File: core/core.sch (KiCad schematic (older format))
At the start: 153 parts, among them K0 KEYSW, K1 KEYSW, K10 KEYSW, K11 KEYSW, K12 KEYSW, K13 KEYSW, K14 KEYSW, K15 KEYSW, K16 KEYSW, K17 KEYSW, K18 KEYSW, K19 KEYSW, K2 KEYSW, K20 KEYSW, K21 KEYSW, K22 KEYSW, K23 KEYSW, K24 KEYSW, K25 KEYSW, K26 KEYSW, K27 KEYSW, K28 KEYSW, K29 KEYSW, K3 KEYSW, K30 KEYSW, K31 KEYSW, K32 KEYSW, K33 KEYSW, K34 KEYSW, K35 KEYSW, K36 KEYSW, K37 KEYSW, K38 KEYSW, K39 KEYSW, K4 KEYSW, K40 KEYSW, K41 KEYSW, K42 KEYSW, K43 KEYSW, K44 KEYSW, K45 KEYSW, K46 KEYSW, K47 KEYSW, K48 KEYSW, K49 KEYSW, K5 KEYSW, K50 KEYSW, K51 KEYSW, K52 KEYSW, K53 KEYSW, K54 KEYSW, K55 KEYSW, K56 KEYSW, K57 KEYSW, K58 KEYSW, K59 KEYSW, K6 KEYSW, K60 KEYSW, K61 KEYSW, K62 KEYSW, K63 KEYSW, K64 KEYSW, K65 KEYSW, K66 KEYSW, K67 KEYSW, K68 KEYSW, K69 KEYSW, K7 KEYSW, K8 KEYSW, K9 KEYSW, U1. Teensy-LC

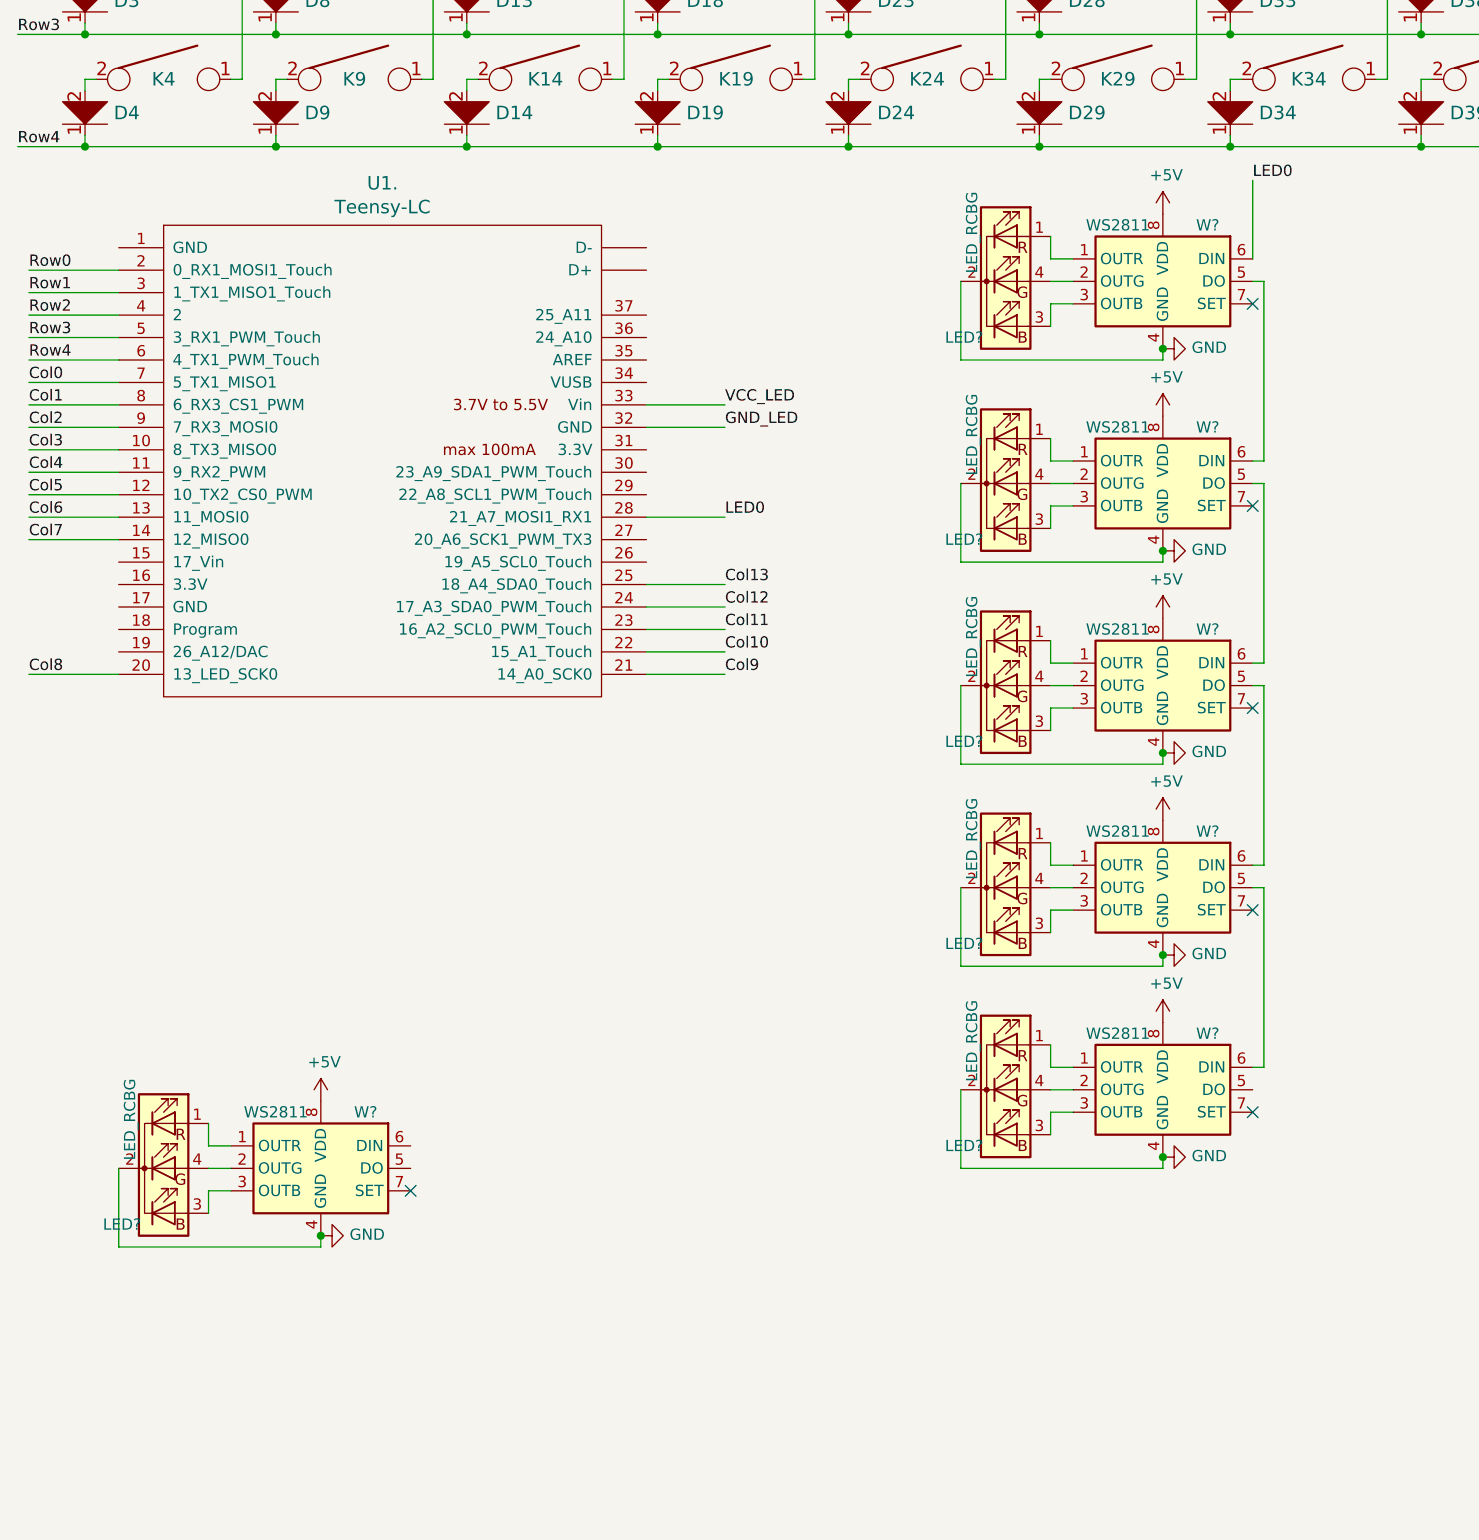
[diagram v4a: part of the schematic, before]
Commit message: Changed pin assignments, cleaned up RGB LEDs
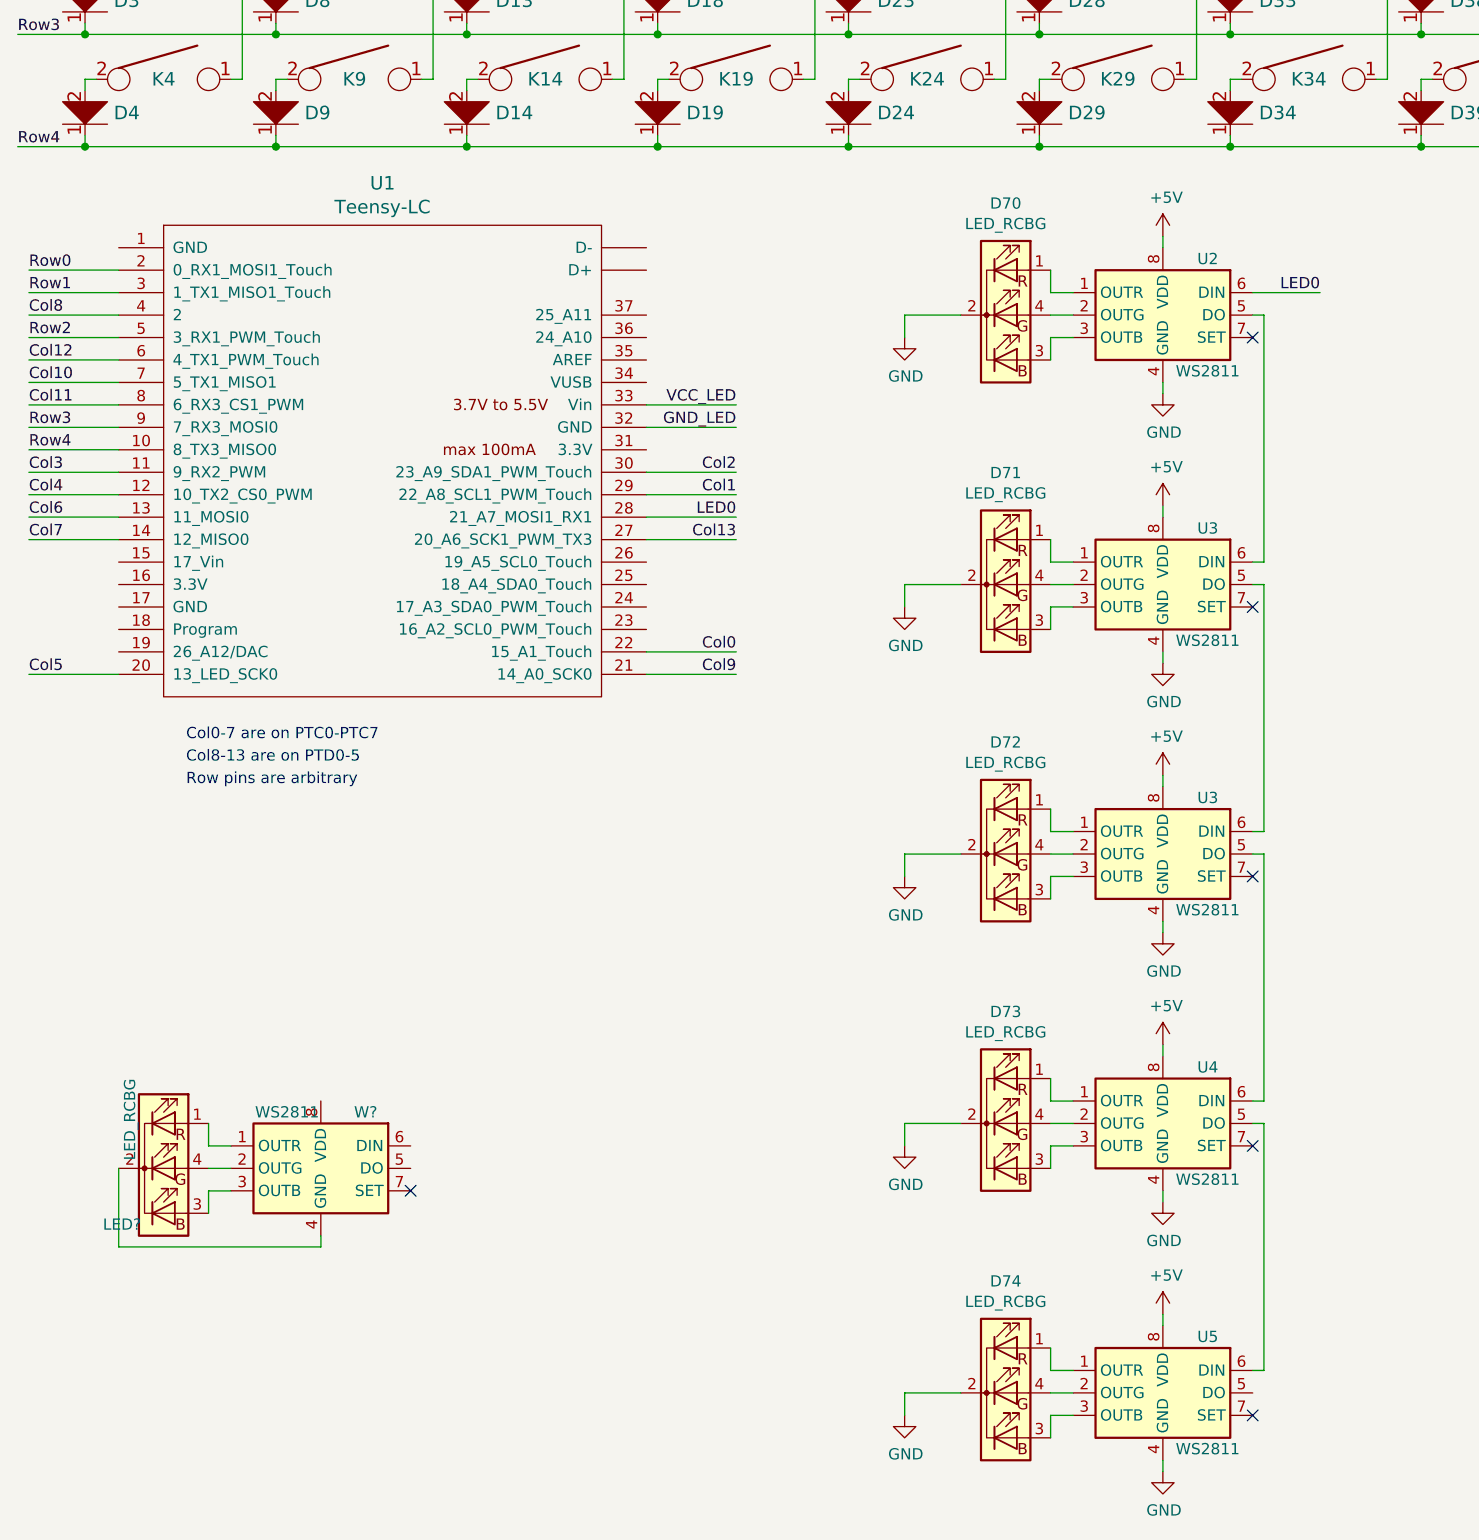
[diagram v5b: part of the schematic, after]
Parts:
- removed LED? (x5): LED_RCBG, Connector_PinHeader_1.00mm:PinHeader_1x04_P1.00mm_Horizontal, symbol Device:LED_RCBG
- removed W? (x5): WS2811, Package_SO:SOIC-8-1EP_3.9x4.9mm_P1.27mm_EP2.29x3mm, symbol Driver_LED:WS2811
- added D70, D71, D72, D73, D74: LED_RCBG, Connector_PinHeader_1.00mm:PinHeader_1x04_P1.00mm_Horizontal, symbol Device:LED_RCBG
- added U2, U3 (x2), U4, U5: WS2811, Package_SO:SOIC-8-1EP_3.9x4.9mm_P1.27mm_EP2.29x3mm, symbol Driver_LED:WS2811
- renumbered U1. to U1
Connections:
- net +5V: now also U2.8 (VDD), U3.8 (VDD), U3.8 (VDD), U4.8 (VDD), U5.8 (VDD); no longer W?.8 (VDD)
- net Col0: now also U1.22 (15_A1_Touch); no longer U1.7 (5_TX1_MISO1)
- net Col1: now also U1.29 (22_A8_SCL1_PWM_Touch); no longer U1.8 (6_RX3_CS1_PWM)
- net Col10: now also U1.7 (5_TX1_MISO1); no longer U1.22 (15_A1_Touch)
- net Col11: now also U1.8 (6_RX3_CS1_PWM); no longer U1.23 (16_A2_SCL0_PWM_Touch)
- net Col12: now also U1.6 (4_TX1_PWM_Touch); no longer U1.24 (17_A3_SDA0_PWM_Touch)
- net Col13: now also U1.27 (20_A6_SCK1_PWM_TX3); no longer U1.25 (18_A4_SDA0_Touch)
- net Col2: now also U1.30 (23_A9_SDA1_PWM_Touch); no longer U1.9 (7_RX3_MOSI0)
- net Col3: now also U1.11 (9_RX2_PWM); no longer U1.10 (8_TX3_MISO0)
- net Col4: now also U1.12 (10_TX2_CS0_PWM); no longer U1.11 (9_RX2_PWM)
- net Col5: now also U1.20 (13_LED_SCK0); no longer U1.12 (10_TX2_CS0_PWM)
- net Col8: now also U1.4 (2); no longer U1.20 (13_LED_SCK0)
- net GND: now also D70.2 (K), D71.2 (K), D72.2 (K), D73.2 (K), D74.2 (K), U2.4 (GND), U3.4 (GND), U3.4 (GND), U4.4 (GND), U5.4 (GND); no longer LED?.2 (K), W?.4 (GND)
- net LED0: now also U2.6 (DIN)
- net Row2: now also U1.5 (3_RX1_PWM_Touch); no longer U1.4 (2)
- net Row3: now also U1.9 (7_RX3_MOSI0); no longer U1.5 (3_RX1_PWM_Touch)
- net Row4: now also U1.10 (8_TX3_MISO0); no longer U1.6 (4_TX1_PWM_Touch)
- new net: D70.1 (RA), U2.1 (OUTR)
- new net: D70.4 (GA), U2.2 (OUTG)
- new net: D70.3 (BA), U2.3 (OUTB)
- new net: U2.5 (DO), U3.6 (DIN)
- new net: D71.1 (RA), U3.1 (OUTR)
- new net: D71.4 (GA), U3.2 (OUTG)
- new net: D71.3 (BA), U3.3 (OUTB)
- new net: U3.5 (DO), U3.6 (DIN)
- new net: D72.1 (RA), U3.1 (OUTR)
- new net: D72.4 (GA), U3.2 (OUTG)
- new net: D72.3 (BA), U3.3 (OUTB)
- new net: U3.5 (DO), U4.6 (DIN)
- new net: D73.1 (RA), U4.1 (OUTR)
- new net: D73.4 (GA), U4.2 (OUTG)
- new net: D73.3 (BA), U4.3 (OUTB)
- new net: U4.5 (DO), U5.6 (DIN)
- new net: D74.1 (RA), U5.1 (OUTR)
- new net: D74.4 (GA), U5.2 (OUTG)
- new net: D74.3 (BA), U5.3 (OUTB)
- new net: LED?.2 (K), W?.4 (GND)
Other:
- note added: "Col0-7 are on PTC0-PTC7"
- note added: "Col8-13 are on PTD0-5"
- note added: "Row pins are arbitrary"

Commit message: LED chain of horrors
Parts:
- removed LED?: LED_RCBG, Connector_PinHeader_1.00mm:PinHeader_1x04_P1.00mm_Horizontal, symbol Device:LED_RCBG
- removed U3 (x2), W?: WS2811, Package_SO:SOIC-8-1EP_3.9x4.9mm_P1.27mm_EP2.29x3mm, symbol Driver_LED:WS2811
- added D100, D101, D102, D103, D104, D105, D106, D107, D108, D109, D110, D111, D112, D113, D114, D115, D116, D117, D118, D119, D120, D121, D122, D123, D124, D125, D126, D127, D128, D129, D130, D131, D132, D133, D134, D135, D136, D137, D138, D139, D140, D75, D76, D77, D78, D79, D80, D81, D82, D83, D84, D85, D86, D87, D88, D89, D90, D91, D92, D93, D94, D95, D96, D97, D98, D99: LED_RCBG, Connector_PinHeader_1.00mm:PinHeader_1x04_P1.00mm_Horizontal, symbol Device:LED_RCBG
- added U10, U11, U12, U13, U14, U15, U16, U17, U18, U19, U20, U21, U22, U23, U24, U25, U26, U27, U28, U29, U3, U30, U31, U32, U33, U34, U35, U36, U37, U38, U39, U40, U41, U42, U43, U44, U45, U46, U47, U48, U49, U50, U51, U52, U53, U54, U55, U56, U57, U58, U59, U6, U60, U61, U62, U63, U64, U65, U66, U67, U68, U69, U7, U70, U71, U72, U8, U9: WS2811, Package_SO:SOIC-8-1EP_3.9x4.9mm_P1.27mm_EP2.29x3mm, symbol Driver_LED:WS2811
- U1: footprint (none) -> teensy:Teensy30_31_32_LC
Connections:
- net Row1 is gone; now on net Col3: D1.1, D11.1, D16.1, D21.1, D26.1, D31.1, D36.1, D41.1, D46.1, D51.1, D56.1, D6.1, D61.1, D66.1, U1.3 (1_TX1_MISO1_Touch)
- net Row2 is gone; now on net Col3: D12.1, D17.1, D2.1, D22.1, D27.1, D32.1, D37.1, D42.1, D47.1, D52.1, D57.1, D62.1, D67.1, D7.1, U1.5 (3_RX1_PWM_Touch)
- net +5V: now also U10.8 (VDD), U11.8 (VDD), U12.8 (VDD), U13.8 (VDD), U14.8 (VDD), U15.8 (VDD), U16.8 (VDD), U17.8 (VDD), U18.8 (VDD), U19.8 (VDD), U20.8 (VDD), U21.8 (VDD), U22.8 (VDD), U23.8 (VDD), U24.8 (VDD), U25.8 (VDD), U26.8 (VDD), U27.8 (VDD), U28.8 (VDD), U29.8 (VDD), U3.8 (VDD), U30.8 (VDD), U31.8 (VDD), U32.8 (VDD), U33.8 (VDD), U34.8 (VDD), U35.8 (VDD), U36.8 (VDD), U37.8 (VDD), U38.8 (VDD), U39.8 (VDD), U40.8 (VDD), U41.8 (VDD), U42.8 (VDD), U43.8 (VDD), U44.8 (VDD), U45.8 (VDD), U46.8 (VDD), U47.8 (VDD), U48.8 (VDD), U49.8 (VDD), U50.8 (VDD), U51.8 (VDD), U52.8 (VDD), U53.8 (VDD), U54.8 (VDD), U55.8 (VDD), U56.8 (VDD), U57.8 (VDD), U58.8 (VDD), U59.8 (VDD), U6.8 (VDD), U60.8 (VDD), U61.8 (VDD), U62.8 (VDD), U63.8 (VDD), U64.8 (VDD), U65.8 (VDD), U66.8 (VDD), U67.8 (VDD), U68.8 (VDD), U69.8 (VDD), U7.8 (VDD), U70.8 (VDD), U71.8 (VDD), U72.8 (VDD), U8.8 (VDD), U9.8 (VDD)
- net GND: now also D100.2 (K), D101.2 (K), D102.2 (K), D103.2 (K), D104.2 (K), D105.2 (K), D106.2 (K), D107.2 (K), D108.2 (K), D109.2 (K), D110.2 (K), D111.2 (K), D112.2 (K), D113.2 (K), D114.2 (K), D115.2 (K), D116.2 (K), D117.2 (K), D118.2 (K), D119.2 (K), D120.2 (K), D121.2 (K), D122.2 (K), D123.2 (K), D124.2 (K), D125.2 (K), D126.2 (K), D127.2 (K), D128.2 (K), D129.2 (K), D130.2 (K), D131.2 (K), D132.2 (K), D133.2 (K), D134.2 (K), D135.2 (K), D136.2 (K), D137.2 (K), D138.2 (K), D139.2 (K), D140.2 (K), D75.2 (K), D76.2 (K), D77.2 (K), D78.2 (K), D79.2 (K), D80.2 (K), D81.2 (K), D82.2 (K), D83.2 (K), D84.2 (K), D85.2 (K), D86.2 (K), D87.2 (K), D88.2 (K), D89.2 (K), D90.2 (K), D91.2 (K), D92.2 (K), D93.2 (K), D94.2 (K), D95.2 (K), D96.2 (K), D97.2 (K), D98.2 (K), D99.2 (K), U10.4 (GND), U11.4 (GND), U12.4 (GND), U13.4 (GND), U14.4 (GND), U15.4 (GND), U16.4 (GND), U17.4 (GND), U18.4 (GND), U19.4 (GND), U20.4 (GND), U21.4 (GND), U22.4 (GND), U23.4 (GND), U24.4 (GND), U25.4 (GND), U26.4 (GND), U27.4 (GND), U28.4 (GND), U29.4 (GND), U3.4 (GND), U30.4 (GND), U31.4 (GND), U32.4 (GND), U33.4 (GND), U34.4 (GND), U35.4 (GND), U36.4 (GND), U37.4 (GND), U38.4 (GND), U39.4 (GND), U40.4 (GND), U41.4 (GND), U42.4 (GND), U43.4 (GND), U44.4 (GND), U45.4 (GND), U46.4 (GND), U47.4 (GND), U48.4 (GND), U49.4 (GND), U50.4 (GND), U51.4 (GND), U52.4 (GND), U53.4 (GND), U54.4 (GND), U55.4 (GND), U56.4 (GND), U57.4 (GND), U58.4 (GND), U59.4 (GND), U6.4 (GND), U60.4 (GND), U61.4 (GND), U62.4 (GND), U63.4 (GND), U64.4 (GND), U65.4 (GND), U66.4 (GND), U67.4 (GND), U68.4 (GND), U69.4 (GND), U7.4 (GND), U70.4 (GND), U71.4 (GND), U72.4 (GND), U8.4 (GND), U9.4 (GND)
- net at U2.5 (DO): now also U3.6 (DIN)
- net at D71.1 (RA): now also U3.1 (OUTR)
- net at D71.4 (GA): now also U3.2 (OUTG)
- net at D71.3 (BA): now also U3.3 (OUTB)
- net at D72.1 (RA): now also U4.1 (OUTR)
- net at D72.4 (GA): now also U4.2 (OUTG)
- net at D72.3 (BA): now also U4.3 (OUTB)
- net at U4.6 (DIN): now also U3.5 (DO)
- net at D73.1 (RA): now also U5.1 (OUTR); no longer U4.1 (OUTR)
- net at D73.4 (GA): now also U5.2 (OUTG); no longer U4.2 (OUTG)
- net at D73.3 (BA): now also U5.3 (OUTB); no longer U4.3 (OUTB)
- net at D74.1 (RA): now also U6.1 (OUTR); no longer U5.1 (OUTR)
- net at D74.4 (GA): now also U6.2 (OUTG); no longer U5.2 (OUTG)
- net at D74.3 (BA): now also U6.3 (OUTB); no longer U5.3 (OUTB)
- net at U5.5 (DO): now also U6.6 (DIN)
- new net: D140.1 (RA), U72.1 (OUTR)
- new net: D140.4 (GA), U72.2 (OUTG)
- new net: D140.3 (BA), U72.3 (OUTB)
- new net: U6.5 (DO), U7.6 (DIN)
- new net: D79.1 (RA), U11.1 (OUTR)
- new net: D79.3 (BA), U11.3 (OUTB)
- new net: D79.4 (GA), U11.2 (OUTG)
- new net: U11.5 (DO), U12.6 (DIN)
- new net: U10.5 (DO), U11.6 (DIN)
- new net: D78.1 (RA), U10.1 (OUTR)
- new net: D78.3 (BA), U10.3 (OUTB)
- new net: D78.4 (GA), U10.2 (OUTG)
- new net: U10.6 (DIN), U9.5 (DO)
- new net: D77.1 (RA), U9.1 (OUTR)
- new net: D77.3 (BA), U9.3 (OUTB)
- new net: D77.4 (GA), U9.2 (OUTG)
- new net: U8.5 (DO), U9.6 (DIN)
- new net: D76.1 (RA), U8.1 (OUTR)
- new net: D76.3 (BA), U8.3 (OUTB)
- new net: D76.4 (GA), U8.2 (OUTG)
- new net: U7.5 (DO), U8.6 (DIN)
- new net: D75.1 (RA), U7.1 (OUTR)
- new net: D75.3 (BA), U7.3 (OUTB)
- new net: D75.4 (GA), U7.2 (OUTG)
- new net: D84.1 (RA), U16.1 (OUTR)
- new net: D84.3 (BA), U16.3 (OUTB)
- new net: D84.4 (GA), U16.2 (OUTG)
- new net: U16.5 (DO), U17.6 (DIN)
- new net: U15.5 (DO), U16.6 (DIN)
- new net: D83.1 (RA), U15.1 (OUTR)
- new net: D83.3 (BA), U15.3 (OUTB)
- new net: D83.4 (GA), U15.2 (OUTG)
- new net: U14.5 (DO), U15.6 (DIN)
- new net: D82.1 (RA), U14.1 (OUTR)
- new net: D82.3 (BA), U14.3 (OUTB)
- new net: D82.4 (GA), U14.2 (OUTG)
- new net: U13.5 (DO), U14.6 (DIN)
- new net: D81.1 (RA), U13.1 (OUTR)
- new net: D81.3 (BA), U13.3 (OUTB)
- new net: D81.4 (GA), U13.2 (OUTG)
- new net: U12.5 (DO), U13.6 (DIN)
- new net: D80.1 (RA), U12.1 (OUTR)
- new net: D80.3 (BA), U12.3 (OUTB)
- new net: D80.4 (GA), U12.2 (OUTG)
- new net: D89.1 (RA), U21.1 (OUTR)
- new net: D89.3 (BA), U21.3 (OUTB)
- new net: D89.4 (GA), U21.2 (OUTG)
- new net: U21.5 (DO), U22.6 (DIN)
- new net: U20.5 (DO), U21.6 (DIN)
- new net: D88.1 (RA), U20.1 (OUTR)
- new net: D88.3 (BA), U20.3 (OUTB)
- new net: D88.4 (GA), U20.2 (OUTG)
- new net: U19.5 (DO), U20.6 (DIN)
- new net: D87.1 (RA), U19.1 (OUTR)
- new net: D87.3 (BA), U19.3 (OUTB)
- new net: D87.4 (GA), U19.2 (OUTG)
- new net: U18.5 (DO), U19.6 (DIN)
- new net: D86.1 (RA), U18.1 (OUTR)
- new net: D86.3 (BA), U18.3 (OUTB)
- new net: D86.4 (GA), U18.2 (OUTG)
- new net: U17.5 (DO), U18.6 (DIN)
- new net: D85.1 (RA), U17.1 (OUTR)
- new net: D85.3 (BA), U17.3 (OUTB)
- new net: D85.4 (GA), U17.2 (OUTG)
- new net: D94.1 (RA), U26.1 (OUTR)
- new net: D94.3 (BA), U26.3 (OUTB)
- new net: D94.4 (GA), U26.2 (OUTG)
- new net: U26.5 (DO), U27.6 (DIN)
- new net: U25.5 (DO), U26.6 (DIN)
- new net: D93.1 (RA), U25.1 (OUTR)
- new net: D93.3 (BA), U25.3 (OUTB)
- new net: D93.4 (GA), U25.2 (OUTG)
- new net: U24.5 (DO), U25.6 (DIN)
- new net: D92.1 (RA), U24.1 (OUTR)
- new net: D92.3 (BA), U24.3 (OUTB)
- new net: D92.4 (GA), U24.2 (OUTG)
- new net: U23.5 (DO), U24.6 (DIN)
- new net: D91.1 (RA), U23.1 (OUTR)
- new net: D91.3 (BA), U23.3 (OUTB)
- new net: D91.4 (GA), U23.2 (OUTG)
- new net: U22.5 (DO), U23.6 (DIN)
- new net: D90.1 (RA), U22.1 (OUTR)
- new net: D90.3 (BA), U22.3 (OUTB)
- new net: D90.4 (GA), U22.2 (OUTG)
- new net: D99.1 (RA), U31.1 (OUTR)
- new net: D99.3 (BA), U31.3 (OUTB)
- new net: D99.4 (GA), U31.2 (OUTG)
- new net: U31.5 (DO), U32.6 (DIN)
- new net: U30.5 (DO), U31.6 (DIN)
- new net: D98.1 (RA), U30.1 (OUTR)
- new net: D98.3 (BA), U30.3 (OUTB)
- new net: D98.4 (GA), U30.2 (OUTG)
- new net: U29.5 (DO), U30.6 (DIN)
- new net: D97.1 (RA), U29.1 (OUTR)
- new net: D97.3 (BA), U29.3 (OUTB)
- new net: D97.4 (GA), U29.2 (OUTG)
- new net: U28.5 (DO), U29.6 (DIN)
- new net: D96.1 (RA), U28.1 (OUTR)
- new net: D96.3 (BA), U28.3 (OUTB)
- new net: D96.4 (GA), U28.2 (OUTG)
- new net: U27.5 (DO), U28.6 (DIN)
- new net: D95.1 (RA), U27.1 (OUTR)
- new net: D95.3 (BA), U27.3 (OUTB)
- new net: D95.4 (GA), U27.2 (OUTG)
- new net: D104.1 (RA), U36.1 (OUTR)
- new net: D104.3 (BA), U36.3 (OUTB)
- new net: D104.4 (GA), U36.2 (OUTG)
- new net: U36.5 (DO), U37.6 (DIN)
- new net: U35.5 (DO), U36.6 (DIN)
- new net: D103.1 (RA), U35.1 (OUTR)
- new net: D103.3 (BA), U35.3 (OUTB)
- new net: D103.4 (GA), U35.2 (OUTG)
- new net: U34.5 (DO), U35.6 (DIN)
- new net: D102.1 (RA), U34.1 (OUTR)
- new net: D102.3 (BA), U34.3 (OUTB)
- new net: D102.4 (GA), U34.2 (OUTG)
- new net: U33.5 (DO), U34.6 (DIN)
- new net: D101.1 (RA), U33.1 (OUTR)
- new net: D101.3 (BA), U33.3 (OUTB)
- new net: D101.4 (GA), U33.2 (OUTG)
- new net: U32.5 (DO), U33.6 (DIN)
- new net: D100.1 (RA), U32.1 (OUTR)
- new net: D100.3 (BA), U32.3 (OUTB)
- new net: D100.4 (GA), U32.2 (OUTG)
- new net: D109.1 (RA), U41.1 (OUTR)
- new net: D109.3 (BA), U41.3 (OUTB)
- new net: D109.4 (GA), U41.2 (OUTG)
- new net: U41.5 (DO), U42.6 (DIN)
- new net: U40.5 (DO), U41.6 (DIN)
- new net: D108.1 (RA), U40.1 (OUTR)
- new net: D108.3 (BA), U40.3 (OUTB)
- new net: D108.4 (GA), U40.2 (OUTG)
- new net: U39.5 (DO), U40.6 (DIN)
- new net: D107.1 (RA), U39.1 (OUTR)
- new net: D107.3 (BA), U39.3 (OUTB)
- new net: D107.4 (GA), U39.2 (OUTG)
- new net: U38.5 (DO), U39.6 (DIN)
- new net: D106.1 (RA), U38.1 (OUTR)
- new net: D106.3 (BA), U38.3 (OUTB)
- new net: D106.4 (GA), U38.2 (OUTG)
- new net: U37.5 (DO), U38.6 (DIN)
- new net: D105.1 (RA), U37.1 (OUTR)
- new net: D105.3 (BA), U37.3 (OUTB)
- new net: D105.4 (GA), U37.2 (OUTG)
- new net: D114.1 (RA), U46.1 (OUTR)
- new net: D114.3 (BA), U46.3 (OUTB)
- new net: D114.4 (GA), U46.2 (OUTG)
- new net: U46.5 (DO), U47.6 (DIN)
- new net: U45.5 (DO), U46.6 (DIN)
- new net: D113.1 (RA), U45.1 (OUTR)
- new net: D113.3 (BA), U45.3 (OUTB)
- new net: D113.4 (GA), U45.2 (OUTG)
- new net: U44.5 (DO), U45.6 (DIN)
- new net: D112.1 (RA), U44.1 (OUTR)
- new net: D112.3 (BA), U44.3 (OUTB)
- new net: D112.4 (GA), U44.2 (OUTG)
- new net: U43.5 (DO), U44.6 (DIN)
- new net: D111.1 (RA), U43.1 (OUTR)
- new net: D111.3 (BA), U43.3 (OUTB)
- new net: D111.4 (GA), U43.2 (OUTG)
- new net: U42.5 (DO), U43.6 (DIN)
- new net: D110.1 (RA), U42.1 (OUTR)
- new net: D110.3 (BA), U42.3 (OUTB)
- new net: D110.4 (GA), U42.2 (OUTG)
- new net: D119.1 (RA), U51.1 (OUTR)
- new net: D119.3 (BA), U51.3 (OUTB)
- new net: D119.4 (GA), U51.2 (OUTG)
- new net: U51.5 (DO), U52.6 (DIN)
- new net: U50.5 (DO), U51.6 (DIN)
- new net: D118.1 (RA), U50.1 (OUTR)
- new net: D118.3 (BA), U50.3 (OUTB)
- new net: D118.4 (GA), U50.2 (OUTG)
- new net: U49.5 (DO), U50.6 (DIN)
- new net: D117.1 (RA), U49.1 (OUTR)
- new net: D117.3 (BA), U49.3 (OUTB)
- new net: D117.4 (GA), U49.2 (OUTG)
- new net: U48.5 (DO), U49.6 (DIN)
- new net: D116.1 (RA), U48.1 (OUTR)
- new net: D116.3 (BA), U48.3 (OUTB)
- new net: D116.4 (GA), U48.2 (OUTG)
- new net: U47.5 (DO), U48.6 (DIN)
- new net: D115.1 (RA), U47.1 (OUTR)
- new net: D115.3 (BA), U47.3 (OUTB)
- new net: D115.4 (GA), U47.2 (OUTG)
- new net: D124.1 (RA), U56.1 (OUTR)
- new net: D124.3 (BA), U56.3 (OUTB)
- new net: D124.4 (GA), U56.2 (OUTG)
- new net: U56.5 (DO), U57.6 (DIN)
- new net: U55.5 (DO), U56.6 (DIN)
- new net: D123.1 (RA), U55.1 (OUTR)
- new net: D123.3 (BA), U55.3 (OUTB)
- new net: D123.4 (GA), U55.2 (OUTG)
- new net: U54.5 (DO), U55.6 (DIN)
- new net: D122.1 (RA), U54.1 (OUTR)
- new net: D122.3 (BA), U54.3 (OUTB)
- new net: D122.4 (GA), U54.2 (OUTG)
- new net: U53.5 (DO), U54.6 (DIN)
- new net: D121.1 (RA), U53.1 (OUTR)
- new net: D121.3 (BA), U53.3 (OUTB)
- new net: D121.4 (GA), U53.2 (OUTG)
- new net: U52.5 (DO), U53.6 (DIN)
- new net: D120.1 (RA), U52.1 (OUTR)
- new net: D120.3 (BA), U52.3 (OUTB)
- new net: D120.4 (GA), U52.2 (OUTG)
- new net: D129.1 (RA), U61.1 (OUTR)
- new net: D129.3 (BA), U61.3 (OUTB)
- new net: D129.4 (GA), U61.2 (OUTG)
- new net: U61.5 (DO), U62.6 (DIN)
- new net: U60.5 (DO), U61.6 (DIN)
- new net: D128.1 (RA), U60.1 (OUTR)
- new net: D128.3 (BA), U60.3 (OUTB)
- new net: D128.4 (GA), U60.2 (OUTG)
- new net: U59.5 (DO), U60.6 (DIN)
- new net: D127.1 (RA), U59.1 (OUTR)
- new net: D127.3 (BA), U59.3 (OUTB)
- new net: D127.4 (GA), U59.2 (OUTG)
- new net: U58.5 (DO), U59.6 (DIN)
- new net: D126.1 (RA), U58.1 (OUTR)
- new net: D126.3 (BA), U58.3 (OUTB)
- new net: D126.4 (GA), U58.2 (OUTG)
- new net: U57.5 (DO), U58.6 (DIN)
- new net: D125.1 (RA), U57.1 (OUTR)
- new net: D125.3 (BA), U57.3 (OUTB)
- new net: D125.4 (GA), U57.2 (OUTG)
- new net: D134.1 (RA), U66.1 (OUTR)
- new net: D134.3 (BA), U66.3 (OUTB)
- new net: D134.4 (GA), U66.2 (OUTG)
- new net: U66.5 (DO), U67.6 (DIN)
- new net: U65.5 (DO), U66.6 (DIN)
- new net: D133.1 (RA), U65.1 (OUTR)
- new net: D133.3 (BA), U65.3 (OUTB)
- new net: D133.4 (GA), U65.2 (OUTG)
- new net: U64.5 (DO), U65.6 (DIN)
- new net: D132.1 (RA), U64.1 (OUTR)
- new net: D132.3 (BA), U64.3 (OUTB)
- new net: D132.4 (GA), U64.2 (OUTG)
- new net: U63.5 (DO), U64.6 (DIN)
- new net: D131.1 (RA), U63.1 (OUTR)
- new net: D131.3 (BA), U63.3 (OUTB)
- new net: D131.4 (GA), U63.2 (OUTG)
- new net: U62.5 (DO), U63.6 (DIN)
- new net: D130.1 (RA), U62.1 (OUTR)
- new net: D130.3 (BA), U62.3 (OUTB)
- new net: D130.4 (GA), U62.2 (OUTG)
- new net: D139.1 (RA), U71.1 (OUTR)
- new net: D139.3 (BA), U71.3 (OUTB)
- new net: D139.4 (GA), U71.2 (OUTG)
- new net: U70.5 (DO), U71.6 (DIN)
- new net: D138.1 (RA), U70.1 (OUTR)
- new net: D138.3 (BA), U70.3 (OUTB)
- new net: D138.4 (GA), U70.2 (OUTG)
- new net: U69.5 (DO), U70.6 (DIN)
- new net: D137.1 (RA), U69.1 (OUTR)
- new net: D137.3 (BA), U69.3 (OUTB)
- new net: D137.4 (GA), U69.2 (OUTG)
- new net: U68.5 (DO), U69.6 (DIN)
- new net: D136.1 (RA), U68.1 (OUTR)
- new net: D136.3 (BA), U68.3 (OUTB)
- new net: D136.4 (GA), U68.2 (OUTG)
- new net: U67.5 (DO), U68.6 (DIN)
- new net: D135.1 (RA), U67.1 (OUTR)
- new net: D135.3 (BA), U67.3 (OUTB)
- new net: D135.4 (GA), U67.2 (OUTG)
- no-connect marks 6 -> 71
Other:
- moved on the sheet: D70, U1, U2

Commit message: add new sheet for keymatrix, rearrange keymatrix, resize sheets
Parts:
- removed D0, D1, D10, D11, D12, D13, D14, D15, D16, D17, D18, D19, D2, D20, D21, D22, D23, D24, D25, D26, D27, D28, D29, D3, D30, D31, D32, D33, D34, D35, D36, D37, D38, D39, D4, D40, D41, D42, D43, D44, D45, D46, D47, D48, D49, D5, D50, D51, D52, D53, D54, D55, D56, D57, D58, D59, D6, D60, D61, D62, D63, D64, D65, D66, D67, D68, D69, D7, D8, D9: D, keyboard_parts:D_SOD123_axial, symbol core-rescue:D-keyboard_parts
- removed K0, K1, K10, K11, K12, K13, K14, K15, K16, K17, K18, K19, K2, K20, K21, K22, K23, K24, K25, K26, K27, K28, K29, K3, K30, K31, K32, K33, K34, K35, K36, K37, K38, K39, K4, K40, K41, K42, K43, K44, K45, K46, K47, K48, K49, K5, K50, K51, K52, K53, K54, K55, K56, K57, K58, K59, K6, K60, K61, K62, K63, K64, K65, K66, K67, K68, K69, K7, K8, K9: KEYSW, keyswitches:Kailh_socket, symbol core-rescue:KEYSW-keyboard_parts
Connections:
- net Col3: no longer U1.3 (1_TX1_MISO1_Touch), U1.5 (3_RX1_PWM_Touch)
- new net Row1: U1.3 (1_TX1_MISO1_Touch)
- new net Row2: U1.5 (3_RX1_PWM_Touch)
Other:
- moved on the sheet: D100, D101, D102, D103, D104, D105, D106, D107, D108, D109, D110, D111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

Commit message: move LEDs into their own sheets
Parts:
- removed D100, D101, D102, D103, D104, D105, D106, D107, D108, D109, D110, D111, D112, D113, D114, D115, D116, D117, D118, D119, D120, D121, D122, D123, D124, D125, D126, D127, D128, D129, D130, D131, D132, D133, D134, D135, D136, D137, D138, D139, D70, D71, D72, D73, D74, D75, D76, D77, D78, D79, D80, D81, D82, D83, D84, D85, D86, D87, D88, D89, D90, D91, D92, D93, D94, D95, D96, D97, D98, D99: LED_RCBG, Connector_PinHeader_1.00mm:PinHeader_1x04_P1.00mm_Horizontal, symbol Device:LED_RCBG
- removed U10, U11, U12, U13, U14, U15, U16, U17, U18, U19, U2, U20, U21, U22, U23, U24, U25, U26, U27, U28, U29, U3, U30, U31, U32, U33, U34, U35, U36, U37, U38, U39, U4, U40, U41, U42, U43, U44, U45, U46, U47, U48, U49, U5, U50, U51, U52, U53, U54, U55, U56, U57, U58, U59, U6, U60, U61, U62, U63, U64, U65, U66, U67, U68, U69, U7, U70, U71, U8, U9: WS2811, Package_SO:SOIC-8-1EP_3.9x4.9mm_P1.27mm_EP2.29x3mm, symbol Driver_LED:WS2811
- renumbered D140 to D?, U72 to U?
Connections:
- no-connect marks 71 -> 1
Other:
- moved on the sheet: D?, U?
